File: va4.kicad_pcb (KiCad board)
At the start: 2 copper layers, 95.8 x 73.1 mm, 19 parts, among them J1 LED, J2 MJ-4PP-9, SW1 RESET_SWITCH, SW2 SW_PUSH, SW3 SW_PUSH, SW4 SW_PUSH, SW5 SW_PUSH, U1 ProMicro

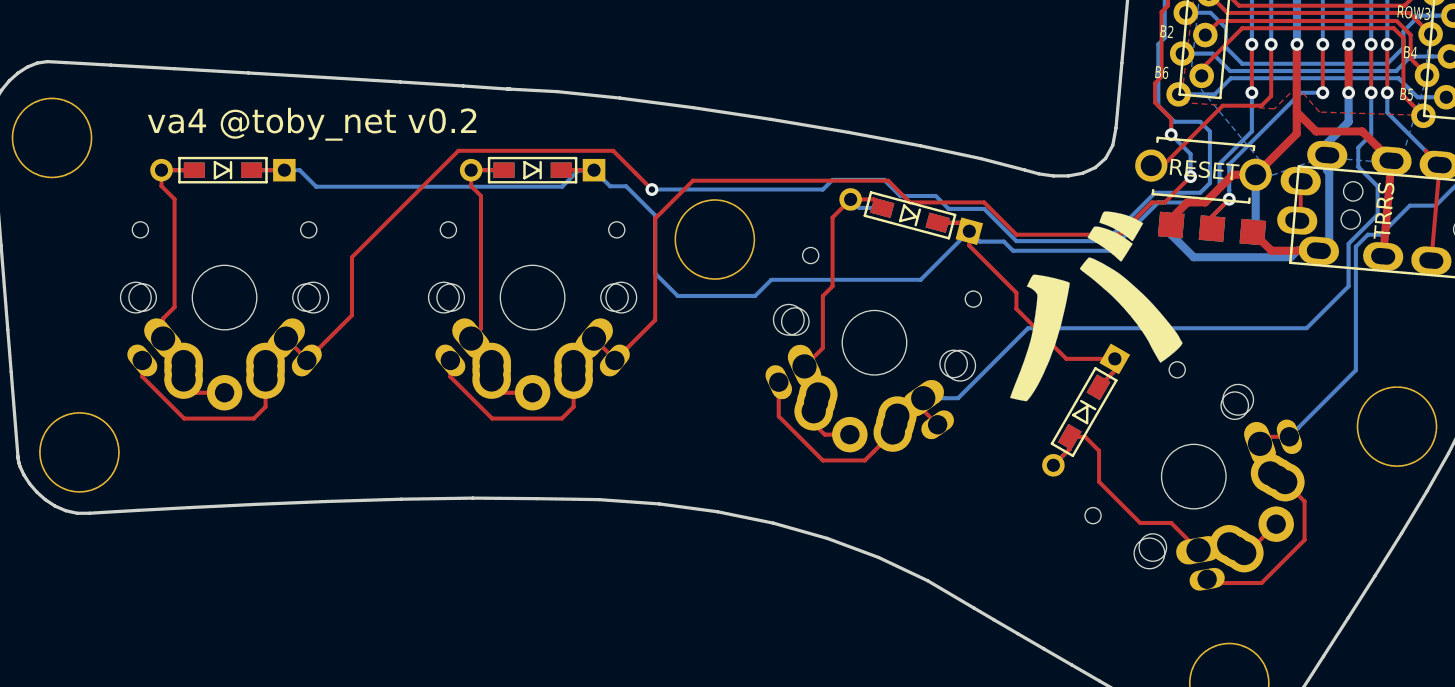
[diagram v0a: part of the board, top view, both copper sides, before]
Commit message: Fix 4th key layout for Kailh Choc key switch(low profile)
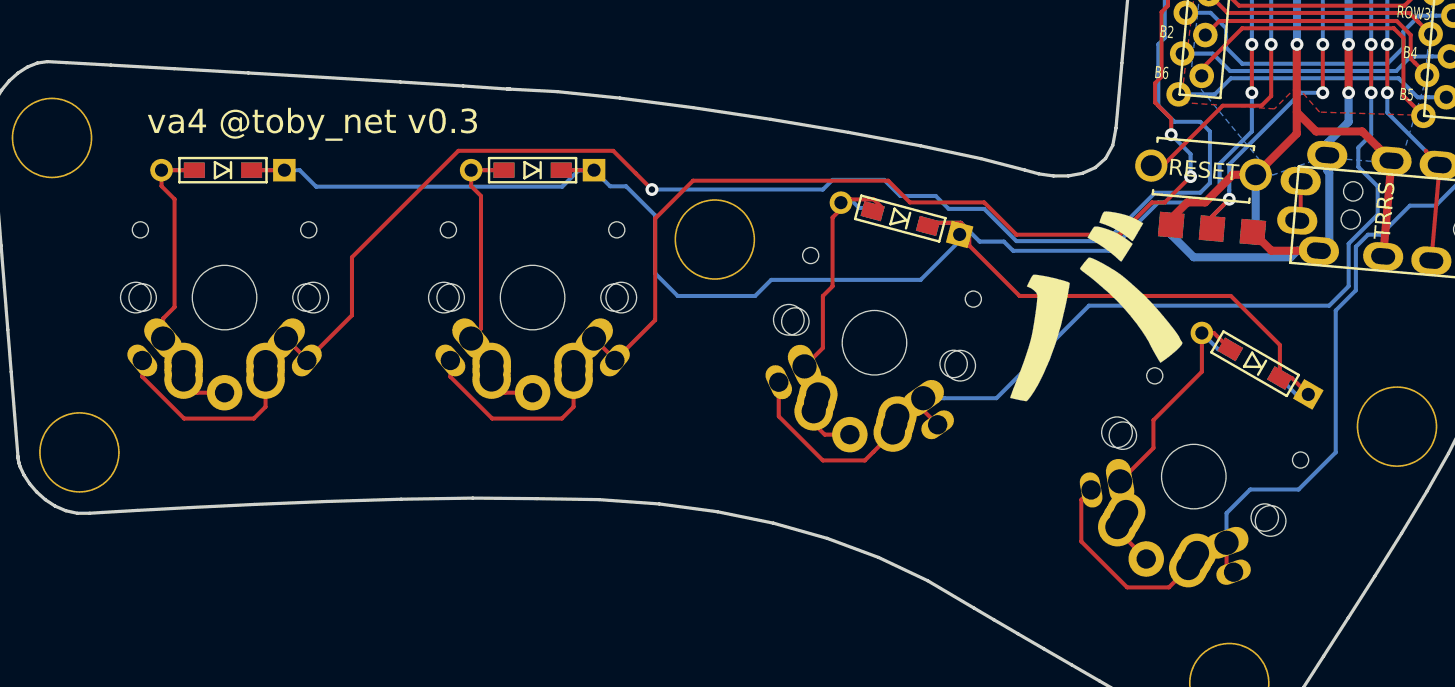
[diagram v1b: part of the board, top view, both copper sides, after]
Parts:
- SW5: footprint kbd:MX_ALPS_PG1350_noLed_1.75u -> kbd:MX_ALPS_PG1350_noLed
- moved D4 11.0 mm to (120.0, 77.8), turned to 150 degrees
- moved D3 0.63 mm to (98.0, 68.8)
- turned SW5 to 150 degrees
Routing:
- net row0: track 140.9 -> 152.2 mm
- net col3: track 70.8 -> 80.6 mm
- net Net-(D4-Pad2): track 21.2 -> 20.4 mm
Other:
- board text added: "va4 @toby_net v0.3"
- board text removed: "va4 @toby_net v0.2"
